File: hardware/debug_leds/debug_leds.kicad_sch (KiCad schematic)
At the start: 29 parts, among them J1 Conn_01x20, J2 Conn_01x20, U1 74HC04, U2 74HC04, U3 74HC04

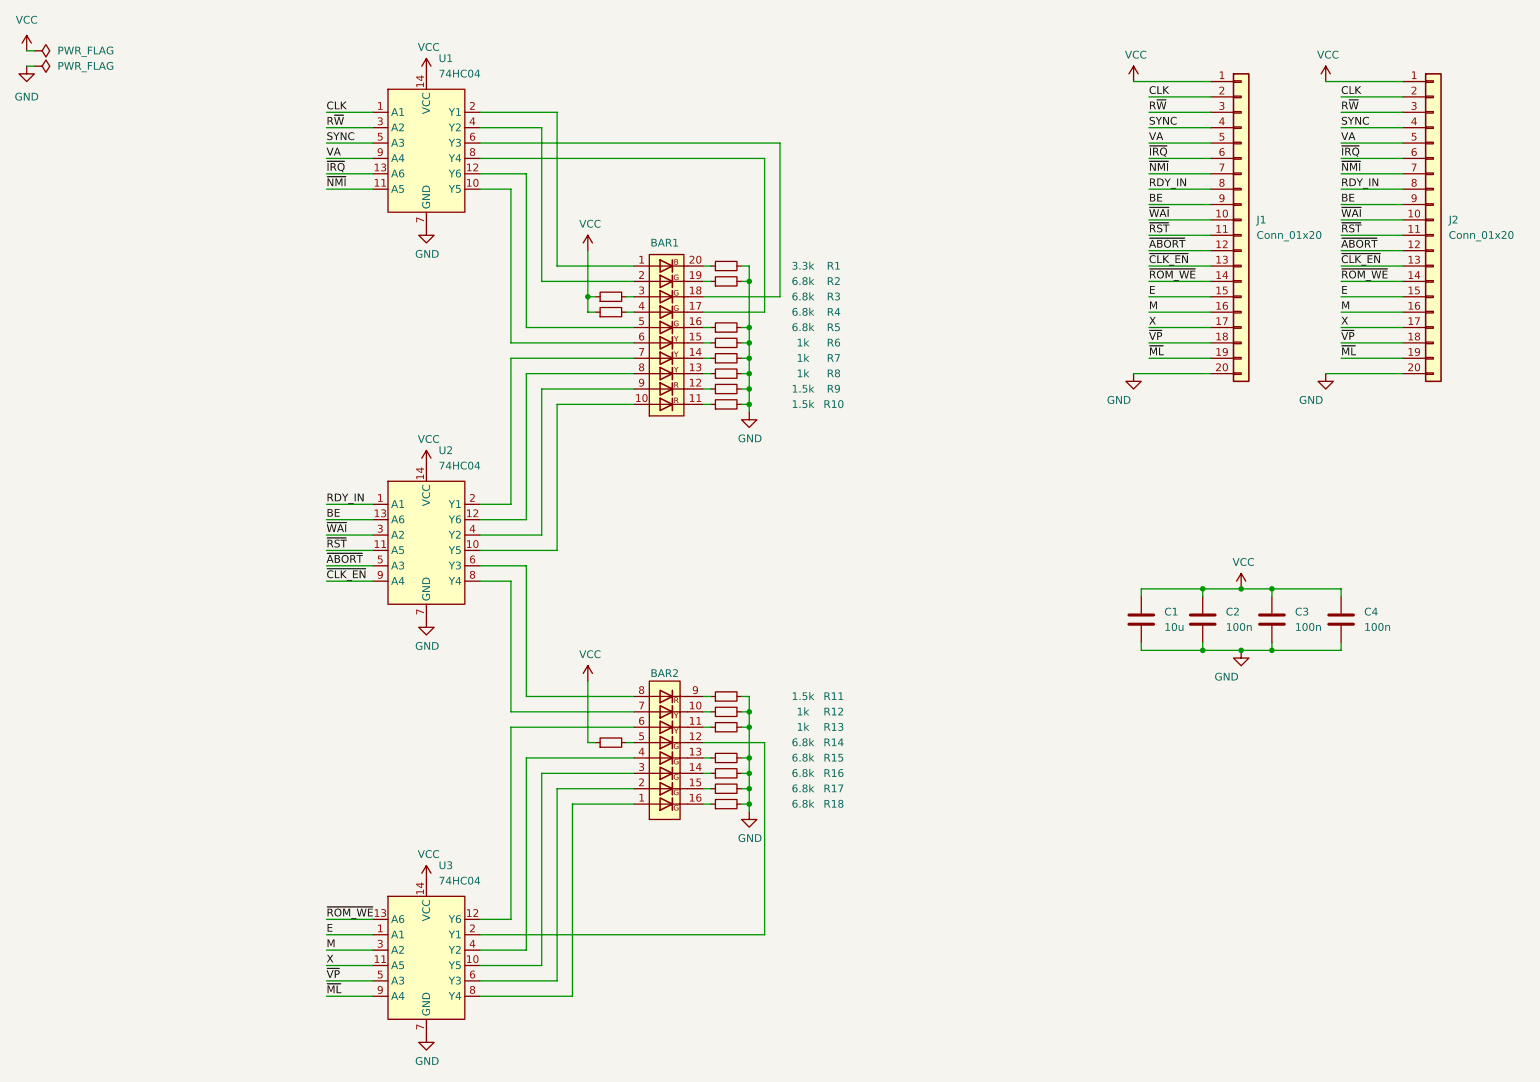
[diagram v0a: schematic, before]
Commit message: Update debug leds
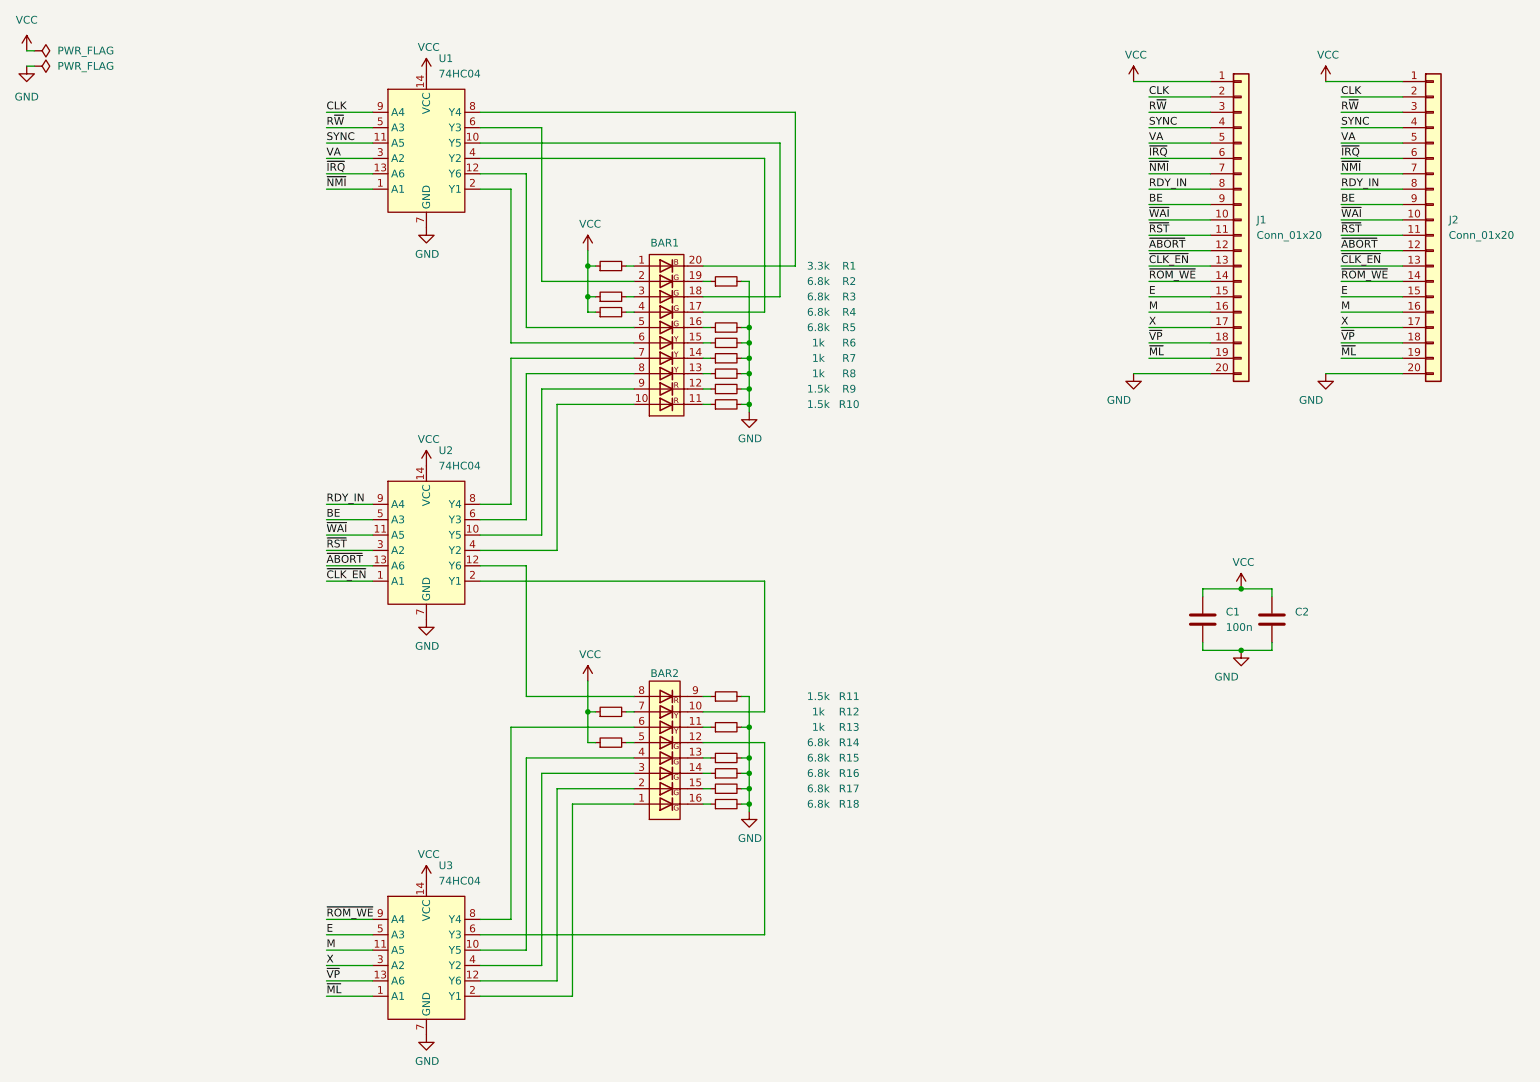
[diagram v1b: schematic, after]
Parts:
- removed C1: 10u, Capacitor_THT:CP_Radial_D4.0mm_P2.00mm, symbol Device:C
- removed C4: 100n, Capacitor_THT:C_Disc_D3.0mm_W1.6mm_P2.50mm, symbol Device:C
- renumbered C2 to C1, C3 to C2
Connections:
- net BE: now also U2.5 (A3); no longer U2.13 (A6)
- net CLK: now also U1.9 (A4); no longer U1.1 (A1)
- net E: now also U3.5 (A3); no longer U3.1 (A1)
- net GND: no longer R1.2, R12.2
- net M: now also U3.11 (A5); no longer U3.3 (A2)
- net RDY_IN: now also U2.9 (A4); no longer U2.1 (A1)
- net R~{W}: now also U1.5 (A3); no longer U1.3 (A2)
- net SYNC: now also U1.11 (A5); no longer U1.5 (A3)
- net VA: now also U1.3 (A2); no longer U1.9 (A4)
- net VCC: now also R1.1, R12.1
- net X: now also U3.3 (A2); no longer U3.11 (A5)
- net ~{ABORT}: now also U2.13 (A6); no longer U2.5 (A3)
- net ~{CLK_EN}: now also U2.1 (A1); no longer U2.9 (A4)
- net ~{ML}: now also U3.1 (A1); no longer U3.9 (A4)
- net ~{NMI}: now also U1.1 (A1); no longer U1.11 (A5)
- net ~{ROM_WE}: now also U3.9 (A4); no longer U3.13 (A6)
- net ~{RST}: now also U2.3 (A2); no longer U2.11 (A5)
- net ~{VP}: now also U3.13 (A6); no longer U3.5 (A3)
- net ~{WAI}: now also U2.11 (A5); no longer U2.3 (A2)
- net at U1.10 (Y5): now also BAR1.18 (K); no longer BAR1.6 (A)
- net at U1.2 (Y1): now also BAR1.6 (A); no longer BAR1.1 (A)
- net at U1.4 (Y2): now also BAR1.17 (K); no longer BAR1.2 (A)
- net at U1.6 (Y3): now also BAR1.2 (A); no longer BAR1.18 (K)
- net at U1.8 (Y4): now also BAR1.20 (K); no longer BAR1.17 (K)
- net at U3.10 (Y5): now also BAR2.4 (A); no longer BAR2.3 (A)
- net at U3.12 (Y6): now also BAR2.2 (A); no longer BAR2.6 (A)
- net at U3.2 (Y1): now also BAR2.1 (A); no longer BAR2.12 (K)
- net at U3.4 (Y2): now also BAR2.3 (A); no longer BAR2.4 (A)
- net at U3.6 (Y3): now also BAR2.12 (K); no longer BAR2.2 (A)
- net at U3.8 (Y4): now also BAR2.6 (A); no longer BAR2.1 (A)
- net at BAR2.10 (K): now also U2.2 (Y1); no longer R12.1
- net at BAR2.7 (A): now also R12.2; no longer U2.8 (Y4)
- net at BAR2.8 (A): now also U2.12 (Y6); no longer U2.6 (Y3)
- net at BAR1.10 (A): now also U2.4 (Y2); no longer U2.10 (Y5)
- net at BAR1.7 (A): now also U2.8 (Y4); no longer U2.2 (Y1)
- net at BAR1.8 (A): now also U2.6 (Y3); no longer U2.12 (Y6)
- net at BAR1.9 (A): now also U2.10 (Y5); no longer U2.4 (Y2)
- new net: BAR1.1 (A), R1.2
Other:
- moved on the sheet: R1, R12
